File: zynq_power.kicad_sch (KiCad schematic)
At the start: 1 part, among them U1 XC7Z007S-1CLG225C

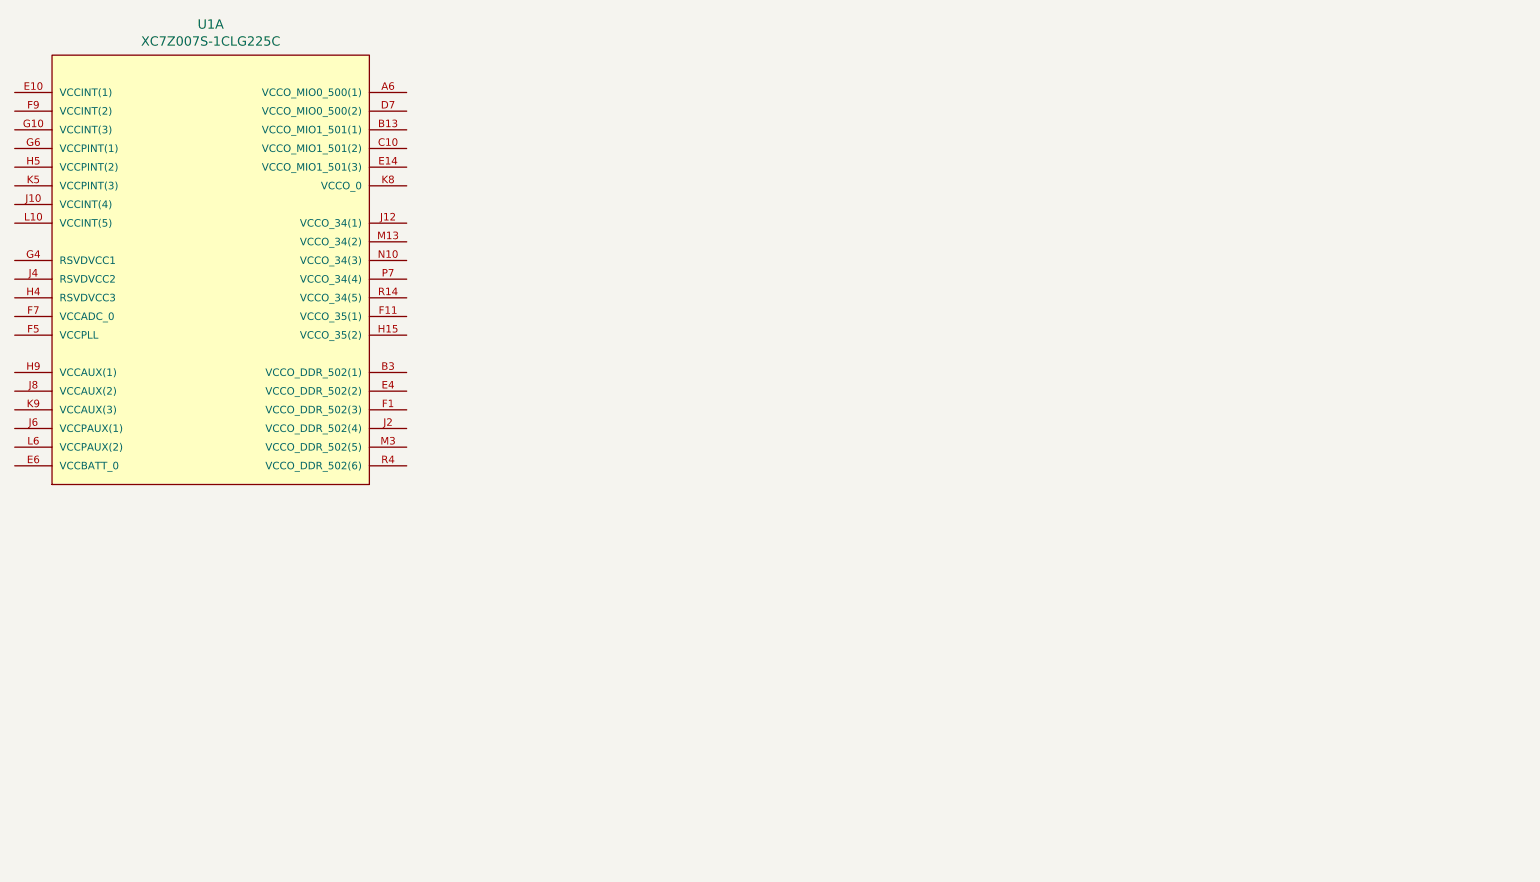
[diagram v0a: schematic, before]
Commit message: zynq_power page: Wire up power pins to rails
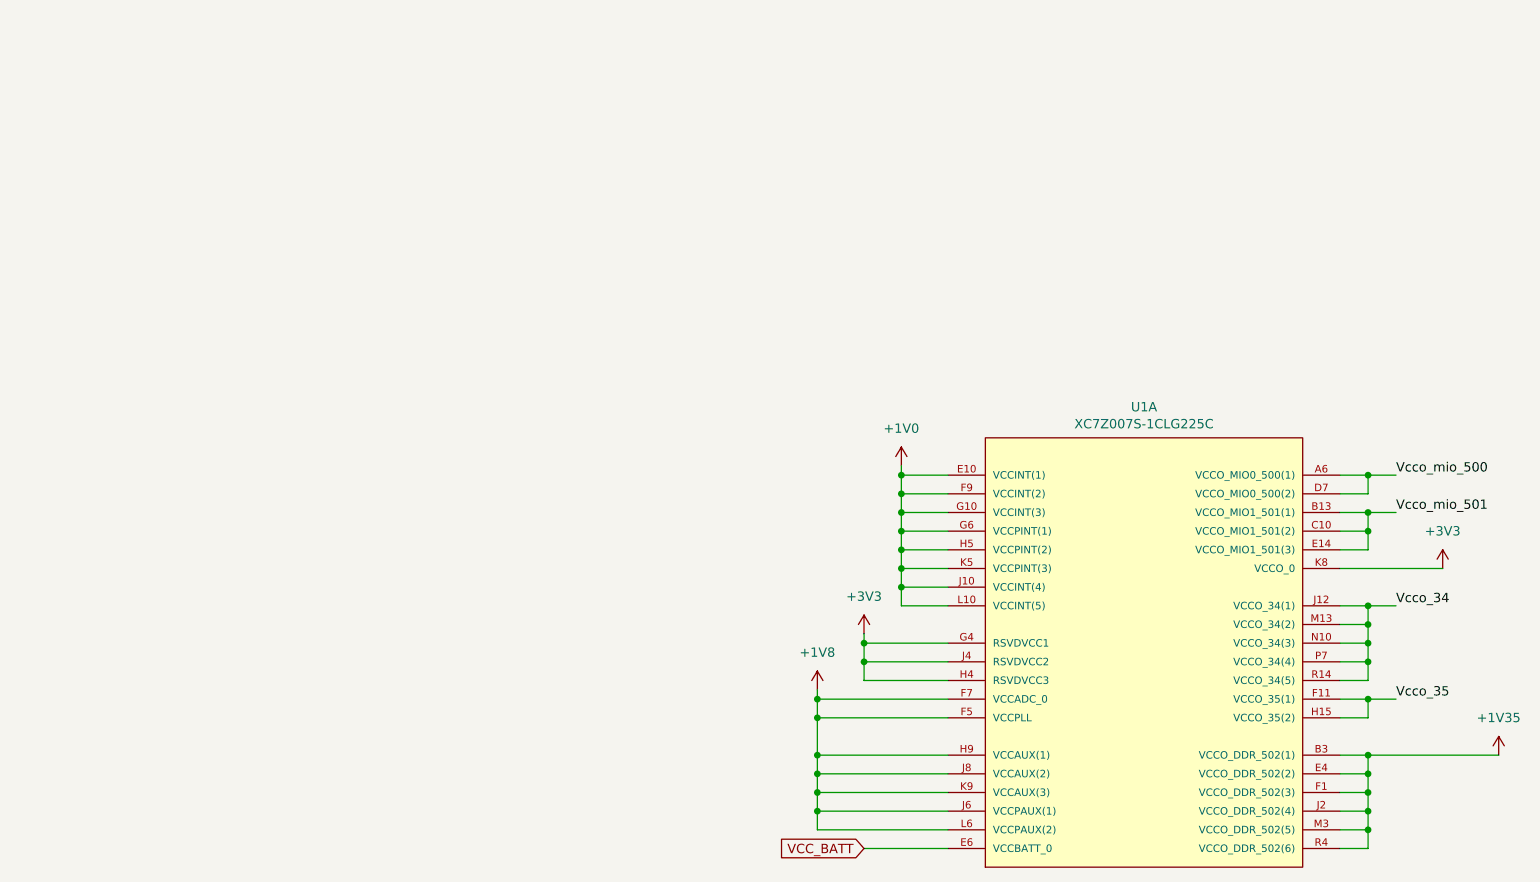
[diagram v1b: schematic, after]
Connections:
- net Vcco_mio_500: now reaches U1.A6 (VCCO_MIO0_500(1))
- net Vcco_mio_500: now also U1.D7 (VCCO_MIO0_500(2))
- net Vcco_mio_501: now reaches U1.B13 (VCCO_MIO1_501(1))
- net Vcco_mio_501: now also U1.C10 (VCCO_MIO1_501(2)), U1.E14 (VCCO_MIO1_501(3))
- net +1V35: now reaches U1.B3 (VCCO_DDR_502(1))
- net +1V35: now also U1.E4 (VCCO_DDR_502(2)), U1.F1 (VCCO_DDR_502(3)), U1.J2 (VCCO_DDR_502(4)), U1.M3 (VCCO_DDR_502(5)), U1.R4 (VCCO_DDR_502(6))
- net +1V0: now reaches U1.E10 (VCCINT(1))
- net +1V0: now also U1.F9 (VCCINT(2)), U1.G10 (VCCINT(3)), U1.G6 (VCCPINT(1)), U1.H5 (VCCPINT(2)), U1.J10 (VCCINT(4)), U1.K5 (VCCPINT(3)), U1.L10 (VCCINT(5))
- net VCC_BATT: now reaches U1.E6 (VCCBATT_0)
- net Vcco_35: now reaches U1.F11 (VCCO_35(1))
- net Vcco_35: now also U1.H15 (VCCO_35(2))
- net +1V8: now reaches U1.F5 (VCCPLL)
- net +1V8: now also U1.F7 (VCCADC_0), U1.H9 (VCCAUX(1)), U1.J6 (VCCPAUX(1)), U1.J8 (VCCAUX(2)), U1.K9 (VCCAUX(3)), U1.L6 (VCCPAUX(2))
- net +3V3: now reaches U1.G4 (RSVDVCC1)
- net +3V3: now also U1.H4 (RSVDVCC3), U1.J4 (RSVDVCC2), U1.K8 (VCCO_0)
- net Vcco_34: now reaches U1.J12 (VCCO_34(1))
- net Vcco_34: now also U1.M13 (VCCO_34(2)), U1.N10 (VCCO_34(3)), U1.P7 (VCCO_34(4)), U1.R14 (VCCO_34(5))
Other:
- moved on the sheet: U1A
